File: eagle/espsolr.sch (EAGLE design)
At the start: 22 parts, among them IC1 ATtiny85

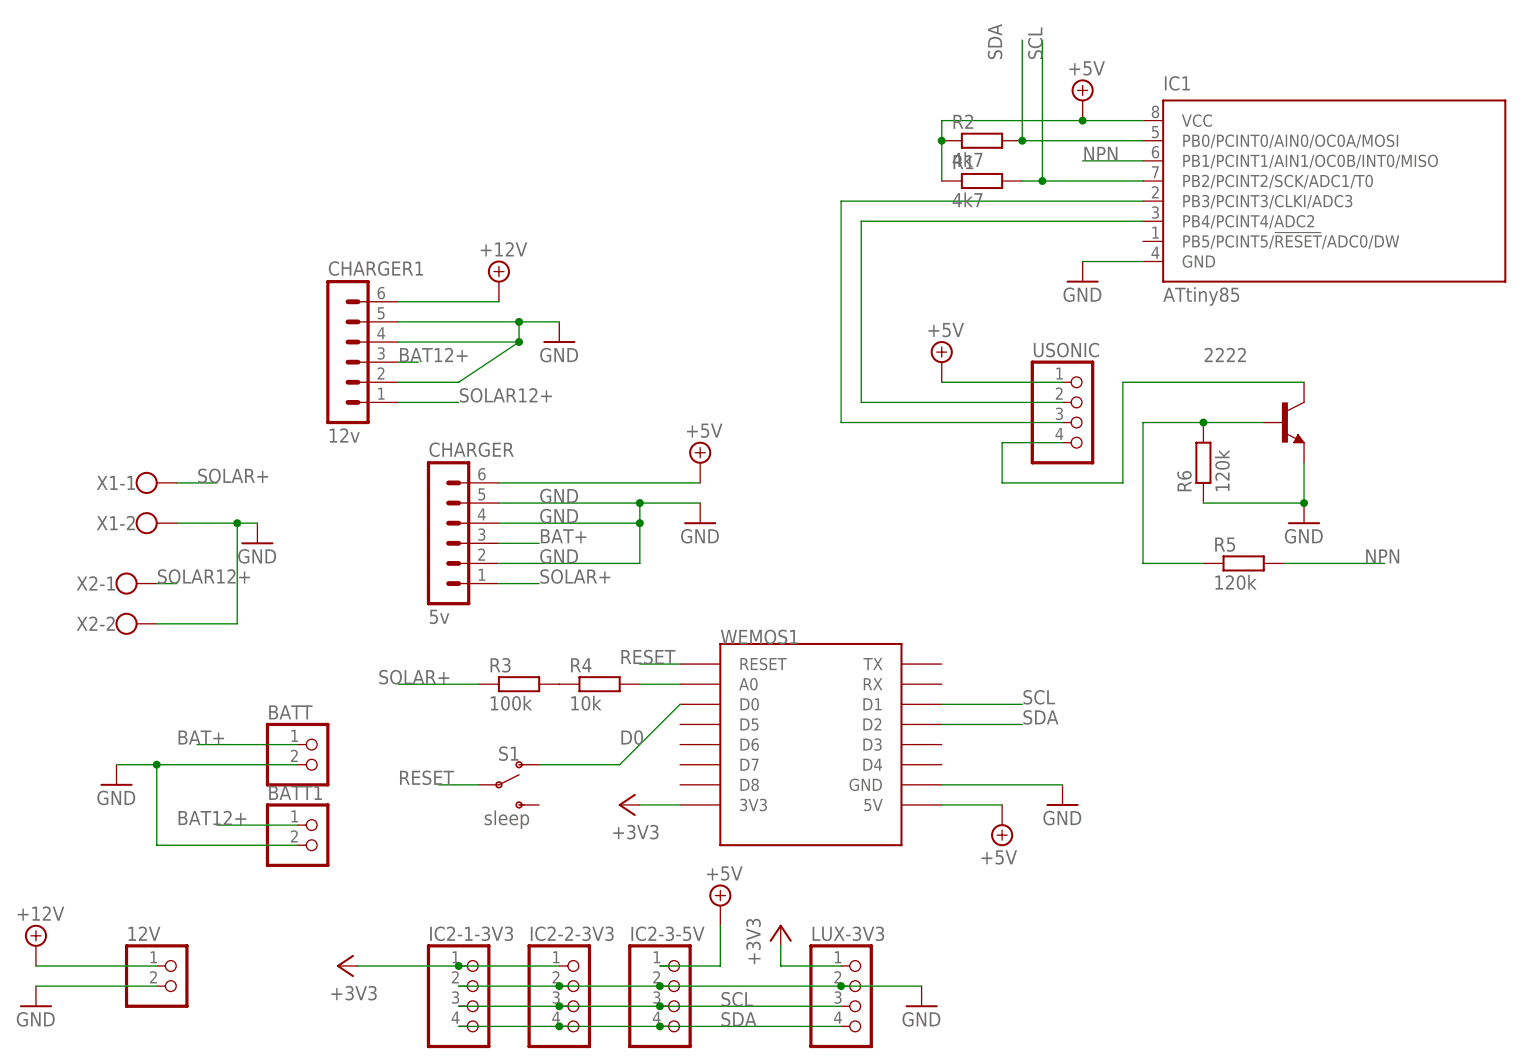
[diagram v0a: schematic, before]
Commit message: removed the 12v i2c from the board - what was i thinking?
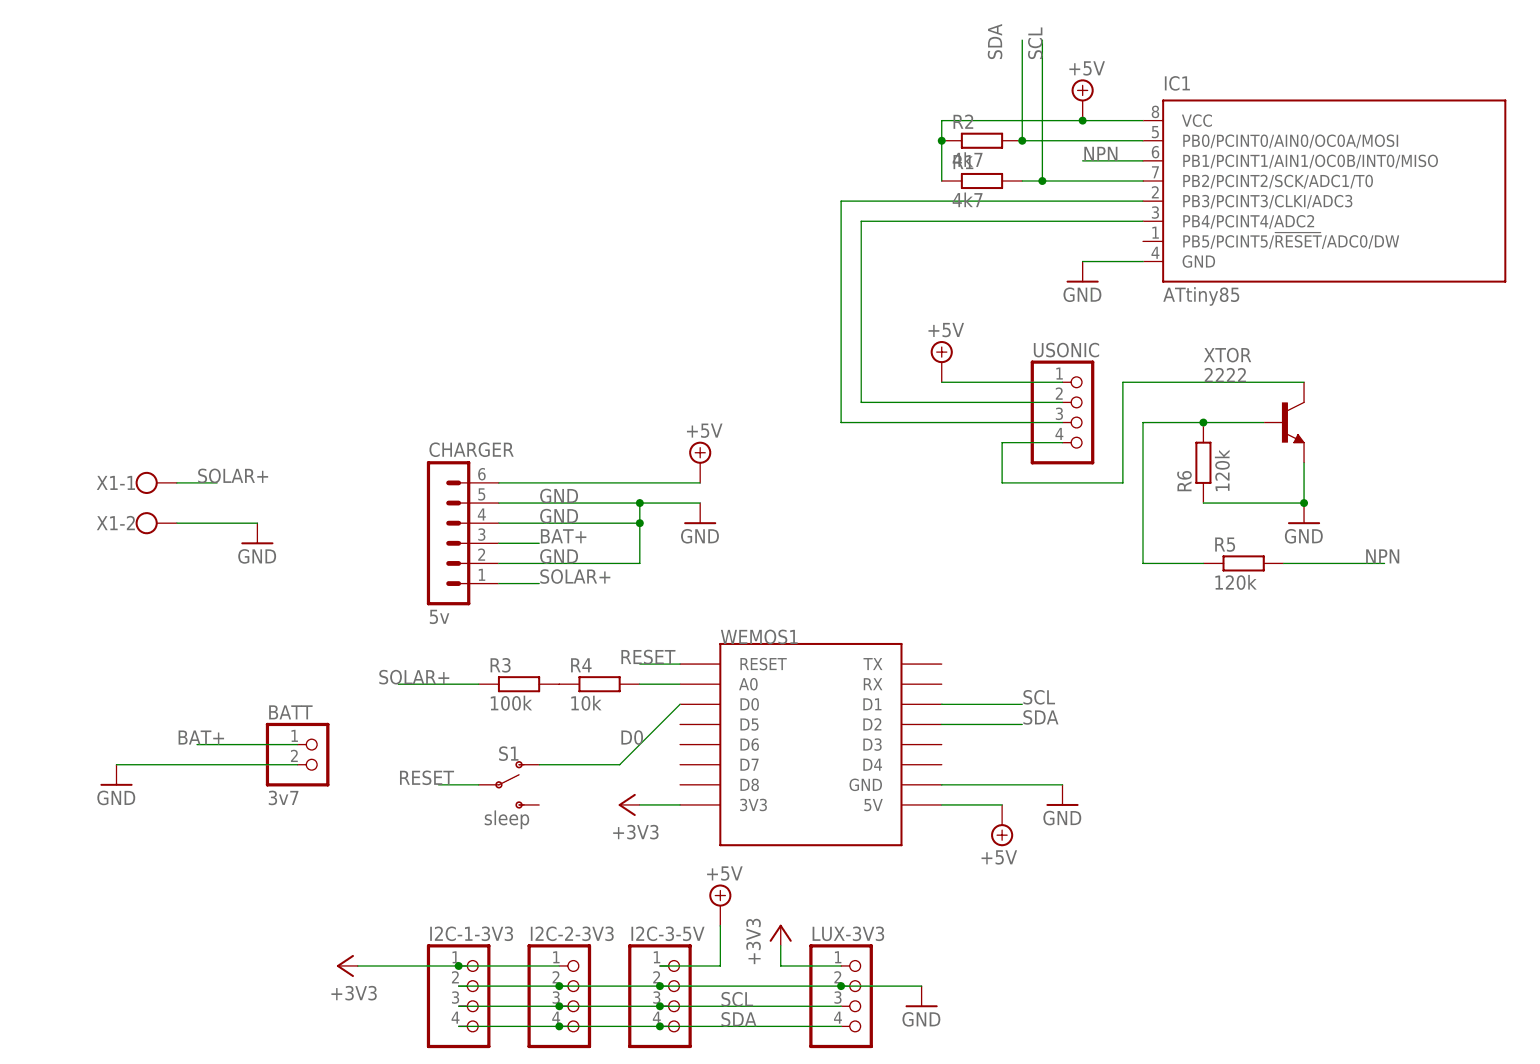
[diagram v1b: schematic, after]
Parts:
- removed 12V, BATT1: (no value), pinhead:PINHD-1X2
- removed CHARGER1: 12v, con-lstb:MA06-1
- removed X2: (no value), con-wago-500:W237-102
- BATT: value (none) -> 3v7
- XTOR: value (none) -> 2222
- renumbered 2222 to XTOR, IC2-1-3V3 to I2C-1-3V3, IC2-2-3V3 to I2C-2-3V3, IC2-3-5V to I2C-3-5V
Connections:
- removed net +12V: 12V.1, CHARGER1.6
- removed net BAT12+: BATT1.1, CHARGER1.3
- removed net SOLAR12+: CHARGER1.1, X2-1.KL
- net GND: no longer 12V.2, BATT1.2, CHARGER1.2, CHARGER1.4, CHARGER1.5, X2-2.KL

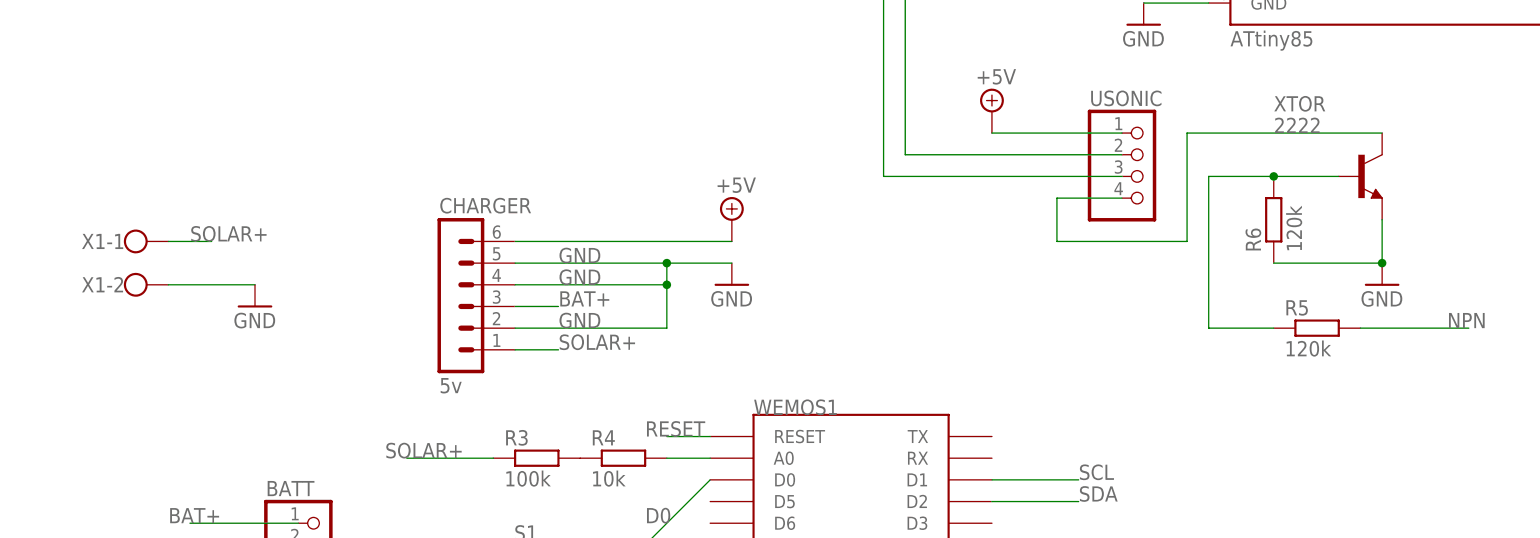
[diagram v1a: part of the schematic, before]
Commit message: updated board and created gerbers
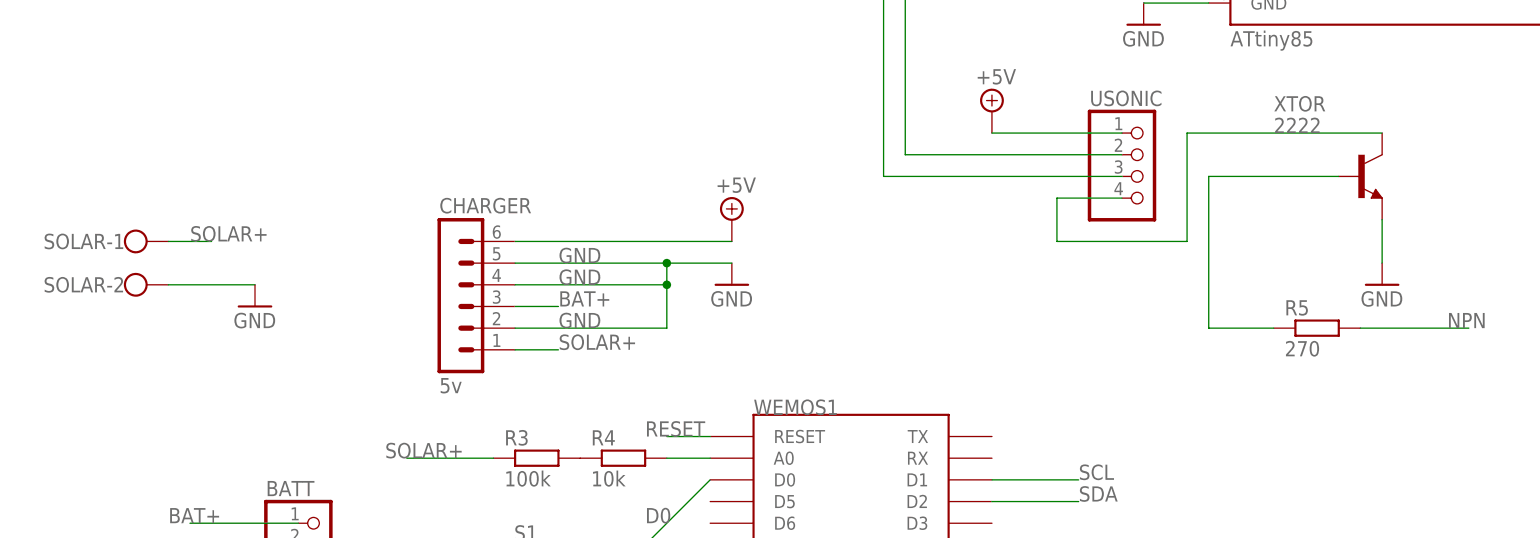
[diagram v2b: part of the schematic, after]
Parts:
- removed R6: 120k, resistor:R-EU_0204/7
- R5: value 120k -> 270
- renumbered X1 to SOLAR
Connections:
- net GND: no longer R6.1
- net N$10: no longer R6.2
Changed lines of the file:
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@@
 <drawing>
 <settings>
-<setting alwaysvectorfont="no"/>
+<setting alwaysvectorfont="yes"/>
 <setting verticaltext="up"/>
 </settings>
@@
 <part name="5V" library="supply2" library_urn="urn:adsk.eagle:library:372" deviceset="+5V" device=""/>
 <part name="GND1" library="supply1" library_urn="urn:adsk.eagle:library:371" deviceset="GND" device=""/>
-<part name="X1" library="con-wago-500" library_urn="urn:adsk.eagle:library:195" deviceset="W237-102" device="" package3d_urn="urn:adsk.eagle:package:10688/1"/>
+<part name="SOLAR" library="con-wago-500" library_urn="urn:adsk.eagle:library:195" deviceset="W237-102" device="" package3d_urn="urn:adsk.eagle:package:10688/1"/>
 <part name="BATT" library="pinhead" library_urn="urn:adsk.eagle:library:325" deviceset="PINHD-1X2" device="" package3d_urn="urn:adsk.eagle:package:22435/2" value="3v7"/>
 <part name="WEMOS1" library="esp8266modules" deviceset="WEMOS-D1-MINI" device=""/>
@@
 <part name="GND7" library="supply1" library_urn="urn:adsk.eagle:library:371" deviceset="GND" device=""/>
 <part name="XTOR" library="transistor-neu-to92" library_urn="urn:adsk.eagle:library:397" deviceset="*-NPN-" device="TO92-EBC" package3d_urn="urn:adsk.eagle:package:28763/2" technology="2N2222" value="2222"/>
-<part name="R5" library="resistor" library_urn="urn:adsk.eagle:library:348" deviceset="R-EU_" device="0204/7" package3d_urn="urn:adsk.eagle:package:25945/1" value="120k"/>
-<part name="R6" library="resistor" library_urn="urn:adsk.eagle:library:348" deviceset="R-EU_" device="0204/7" package3d_urn="urn:adsk.eagle:package:25945/1" value="120k"/>
+<part name="R5" library="resistor" library_urn="urn:adsk.eagle:library:348" deviceset="R-EU_" device="0204/7" package3d_urn="urn:adsk.eagle:package:25945/1" value="270"/>
 <part name="+3V1" library="supply1" library_urn="urn:adsk.eagle:library:371" deviceset="+3V3" device=""/>
 <part name="+3V2" library="supply1" library_urn="urn:adsk.eagle:library:371" deviceset="+3V3" device=""/>
@@
 <instance part="5V" gate="+5V" x="83.82" y="71.12"/>
 <instance part="GND1" gate="1" x="83.82" y="63.5"/>
-<instance part="X1" gate="-1" x="12.7" y="68.58"/>
-<instance part="X1" gate="-2" x="12.7" y="63.5"/>
+<instance part="SOLAR" gate="-1" x="12.7" y="68.58"/>
+<instance part="SOLAR" gate="-2" x="12.7" y="63.5"/>
 <instance part="BATT" gate="G$1" x="35.56" y="33.02"/>
 <instance part="WEMOS1" gate="D1" x="96.52" y="35.56"/>
@@
 <instance part="XTOR" gate="G$1" x="157.48" y="76.2"/>
 <instance part="R5" gate="G$1" x="152.4" y="58.42"/>
-<instance part="R6" gate="G$1" x="147.32" y="71.12" rot="R90"/>
 <instance part="+3V1" gate="G$1" x="73.66" y="27.94" rot="R90"/>
 <instance part="+3V2" gate="G$1" x="38.1" y="7.62" rot="R90"/>
@@
 </segment>
 <segment>
-<pinref part="X1" gate="-2" pin="KL"/>
+<pinref part="SOLAR" gate="-2" pin="KL"/>
 <pinref part="GND2" gate="1" pin="GND"/>
 <wire x1="17.78" y1="63.5" x2="27.94" y2="63.5" width="0.1524" layer="91"/>
@@
 <pinref part="GND7" gate="1" pin="GND"/>
 <wire x1="160.02" y1="66.04" x2="160.02" y2="71.12" width="0.1524" layer="91"/>
-<pinref part="R6" gate="G$1" pin="1"/>
-<wire x1="147.32" y1="66.04" x2="160.02" y2="66.04" width="0.1524" layer="91"/>
-<junction x="160.02" y="66.04"/>
 </segment>
 </net>
@@
 </segment>
 <segment>
-<pinref part="X1" gate="-1" pin="KL"/>
+<pinref part="SOLAR" gate="-1" pin="KL"/>
 <wire x1="17.78" y1="68.58" x2="22.86" y2="68.58" width="0.1524" layer="91"/>
 <label x="20.32" y="68.58" size="1.778" layer="95"/>
@@
 <net name="N$10" class="0">
 <segment>
-<pinref part="R6" gate="G$1" pin="2"/>
 <pinref part="XTOR" gate="G$1" pin="B"/>
-<wire x1="147.32" y1="76.2" x2="154.94" y2="76.2" width="0.1524" layer="91"/>
-<wire x1="147.32" y1="76.2" x2="139.7" y2="76.2" width="0.1524" layer="91"/>
-<junction x="147.32" y="76.2"/>
+<wire x1="154.94" y1="76.2" x2="139.7" y2="76.2" width="0.1524" layer="91"/>
 <wire x1="139.7" y1="76.2" x2="139.7" y2="58.42" width="0.1524" layer="91"/>
 <pinref part="R5" gate="G$1" pin="1"/>

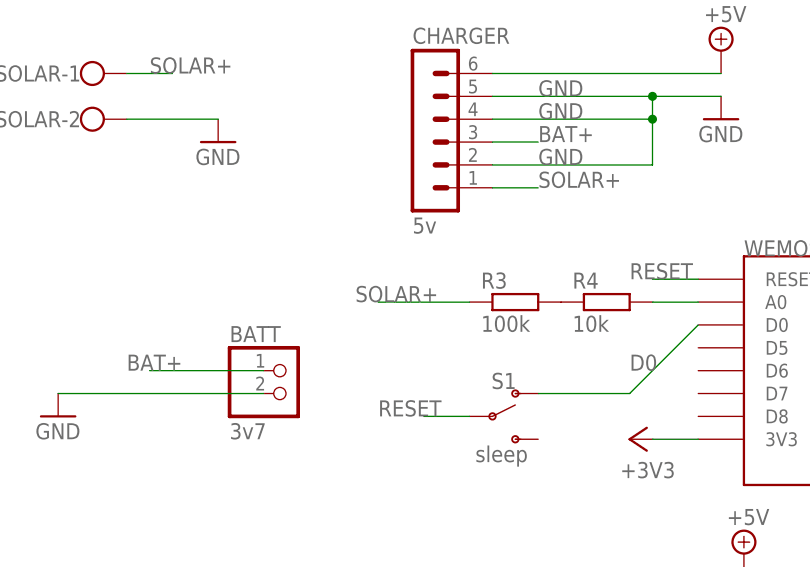
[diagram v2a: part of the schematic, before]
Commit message: fixed the analog pin to battery - duh!
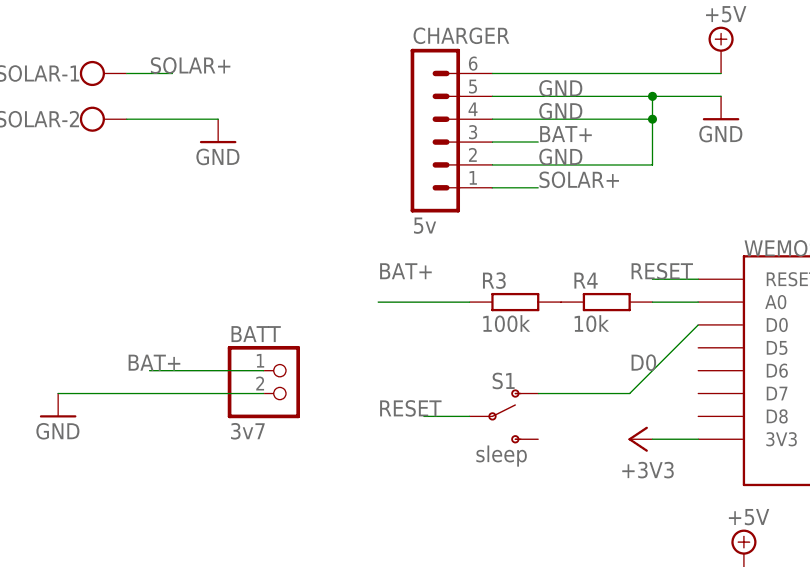
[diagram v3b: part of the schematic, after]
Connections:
- net BAT+: now also R3.1
- net SOLAR+: no longer R3.1
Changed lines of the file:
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@@
 <?xml version="1.0" encoding="utf-8"?>
 <!DOCTYPE eagle SYSTEM "eagle.dtd">
-<eagle version="9.0.1">
+<eagle version="9.1.0">
 <drawing>
 <settings>
@@
 <label x="17.78" y="35.56" size="1.778" layer="95"/>
 </segment>
+<segment>
+<pinref part="R3" gate="G$1" pin="1"/>
+<wire x1="55.88" y1="43.18" x2="45.72" y2="43.18" width="0.1524" layer="91"/>
+<label x="45.72" y="45.72" size="1.778" layer="95"/>
+</segment>
 </net>
 <net name="SOLAR+" class="0">
@@
 <label x="20.32" y="68.58" size="1.778" layer="95"/>
 </segment>
-<segment>
-<wire x1="55.88" y1="43.18" x2="45.72" y2="43.18" width="0.1524" layer="91"/>
-<label x="43.18" y="43.18" size="1.778" layer="95"/>
-<pinref part="R3" gate="G$1" pin="1"/>
-</segment>
 </net>
